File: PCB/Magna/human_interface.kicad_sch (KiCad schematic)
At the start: 1 part, among them J601 Conn_02x10_Counter_Clockwise

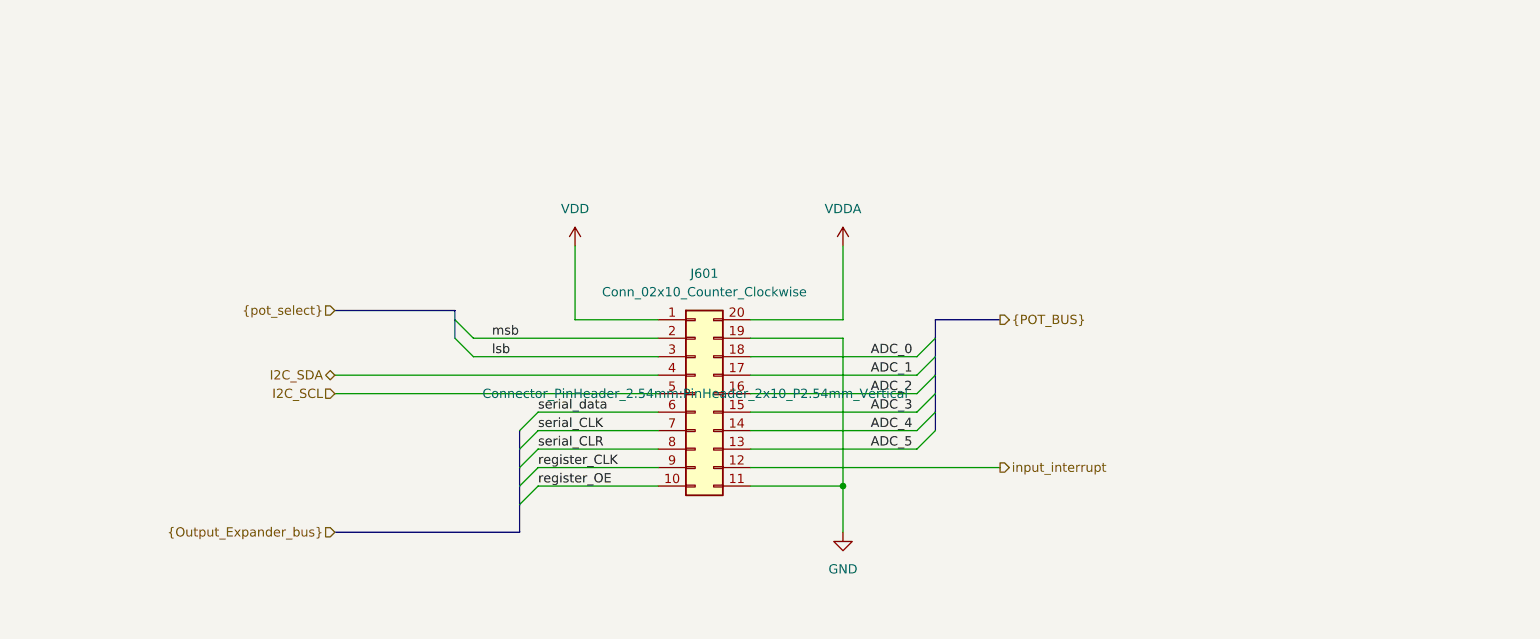
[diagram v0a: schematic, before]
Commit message: Add more traces to the PCB
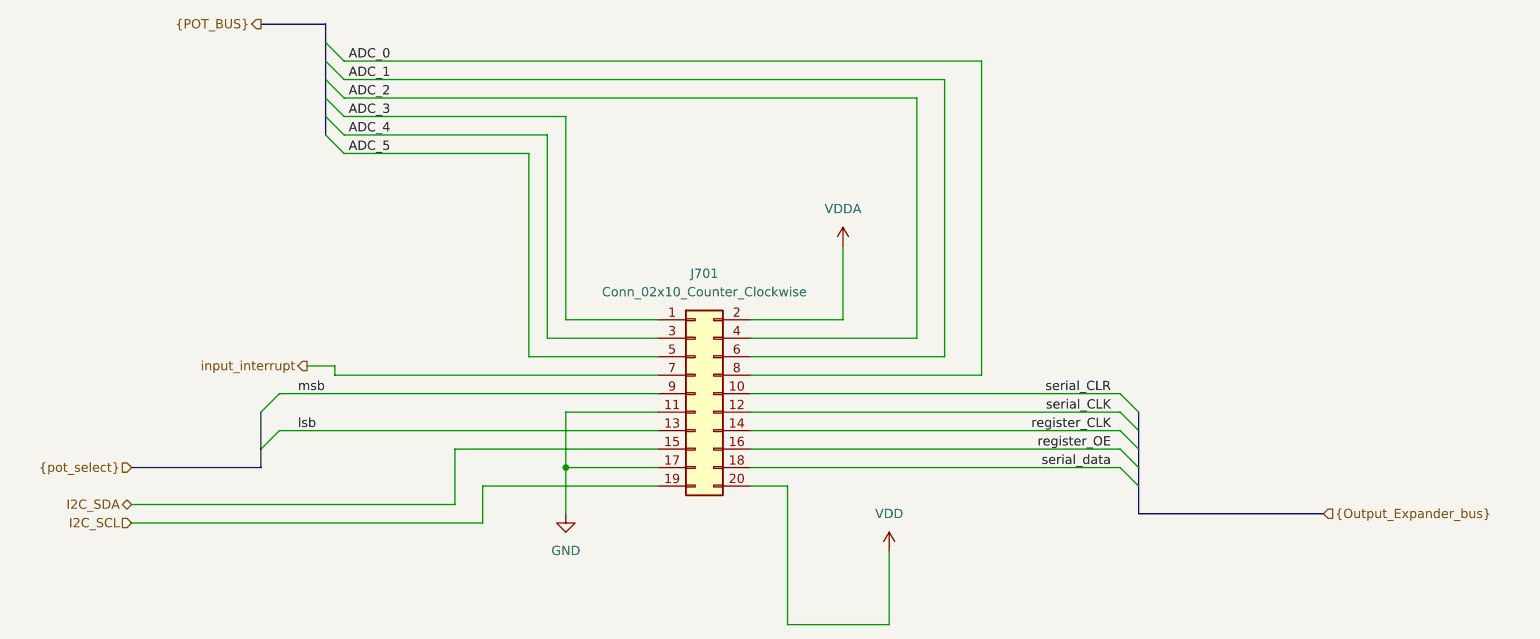
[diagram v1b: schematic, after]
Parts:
- J701: renamed from J601; symbol Connector_Generic:Conn_02x10_Counter_Clockwise -> Connector_Generic:Conn_02x10_Odd_Even
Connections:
- net ADC_0: now also J701.8 (Pin_8); no longer J701.18 (Pin_18)
- net ADC_1: now also J701.6 (Pin_6); no longer J701.17 (Pin_17)
- net ADC_2: now also J701.4 (Pin_4); no longer J701.16 (Pin_16)
- net ADC_3: now also J701.1 (Pin_1); no longer J701.15 (Pin_15)
- net ADC_4: now also J701.3 (Pin_3); no longer J701.14 (Pin_14)
- net ADC_5: now also J701.5 (Pin_5); no longer J701.13 (Pin_13)
- net GND: now also J701.17 (Pin_17); no longer J701.19 (Pin_19)
- net I2C_SCL: now also J701.19 (Pin_19); no longer J701.5 (Pin_5)
- net I2C_SDA: now also J701.15 (Pin_15); no longer J701.4 (Pin_4)
- net VDD: now also J701.20 (Pin_20); no longer J701.1 (Pin_1)
- net VDDA: now also J701.2 (Pin_2); no longer J701.20 (Pin_20)
- net input_interrupt: now also J701.7 (Pin_7); no longer J701.12 (Pin_12)
- net lsb: now also J701.13 (Pin_13); no longer J701.3 (Pin_3)
- net msb: now also J701.9 (Pin_9); no longer J701.2 (Pin_2)
- net register_CLK: now also J701.14 (Pin_14); no longer J701.9 (Pin_9)
- net register_OE: now also J701.16 (Pin_16); no longer J701.10 (Pin_10)
- net serial_CLK: now also J701.12 (Pin_12); no longer J701.7 (Pin_7)
- net serial_CLR: now also J701.10 (Pin_10); no longer J701.8 (Pin_8)
- net serial_data: now also J701.18 (Pin_18); no longer J701.6 (Pin_6)

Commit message: Finish PCB design and added mounting holes
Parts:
- J701: footprint Connector_PinHeader_2.54mm:PinHeader_2x10_P2.54mm_Vertical -> Connector_PinHeader_2.54mm:PinHeader_2x10_P2.54mm_Horizontal
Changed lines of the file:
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@@
       (effects (font (size 1.27 1.27)))
     )
-    (property "Footprint" "Connector_PinHeader_2.54mm:PinHeader_2x10_P2.54mm_Vertical" (at 138.43 72.39 0)
+    (property "Footprint" "Connector_PinHeader_2.54mm:PinHeader_2x10_P2.54mm_Horizontal" (at 138.43 72.39 0)
       (effects (font (size 1.27 1.27)) hide)
     )
